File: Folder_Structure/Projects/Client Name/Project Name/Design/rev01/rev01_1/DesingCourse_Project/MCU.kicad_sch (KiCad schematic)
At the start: 43 parts, among them J3 874380243, J4 874380843, J5 874380343, J6 874380643, U3 STM32F405RGTx, Y1 8MHz

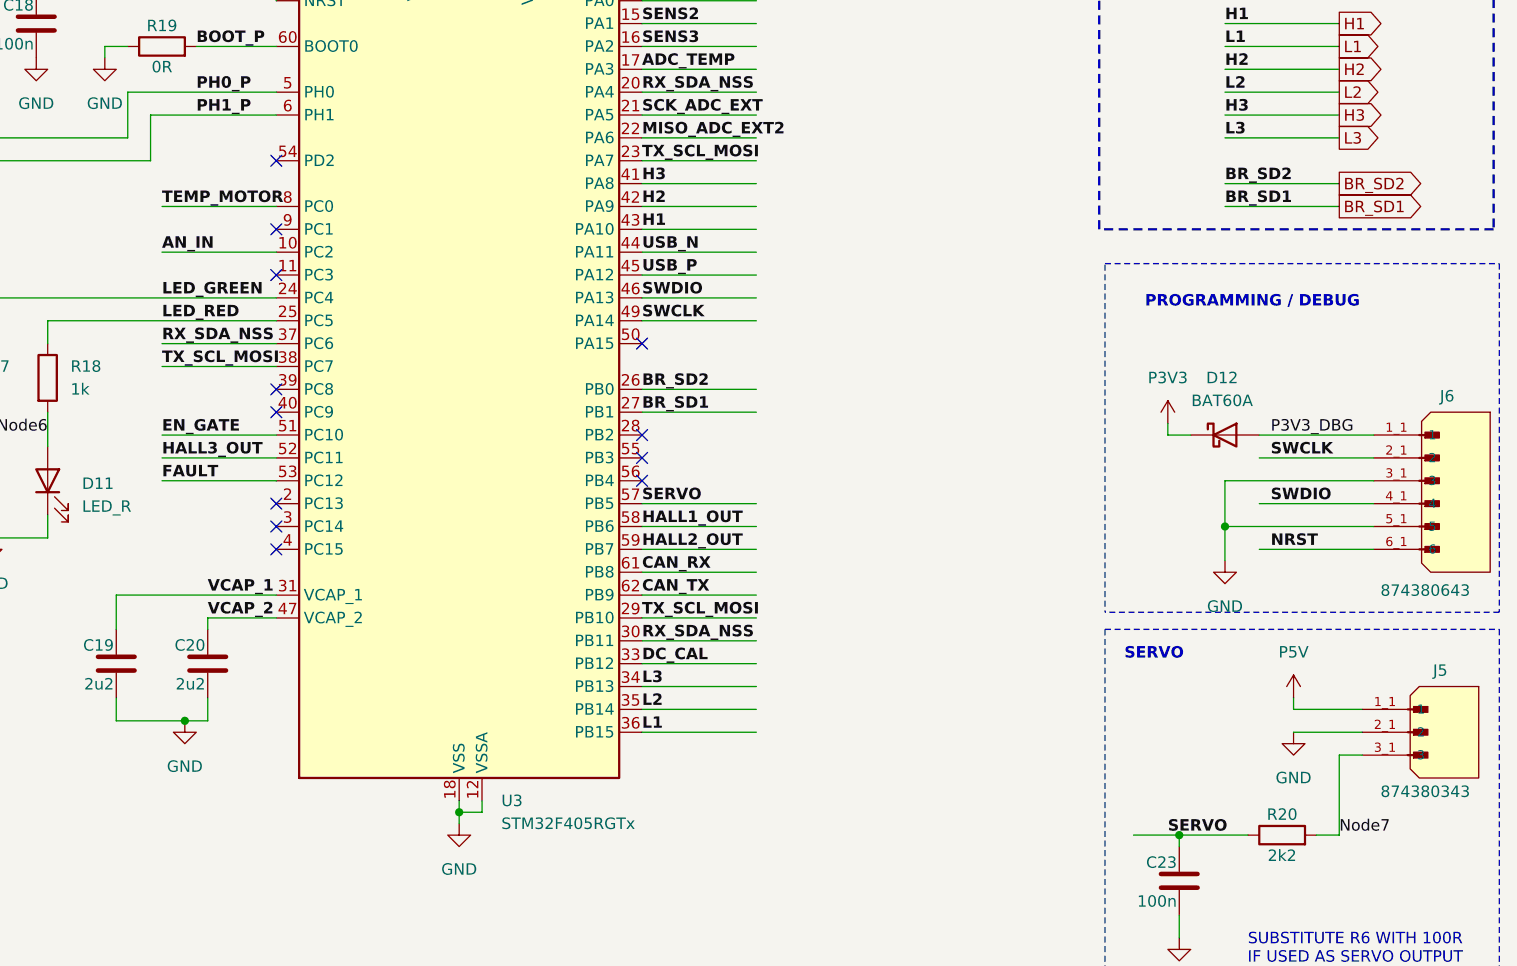
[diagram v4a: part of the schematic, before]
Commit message: Update18
Layout finished, clean up or layout and designators.
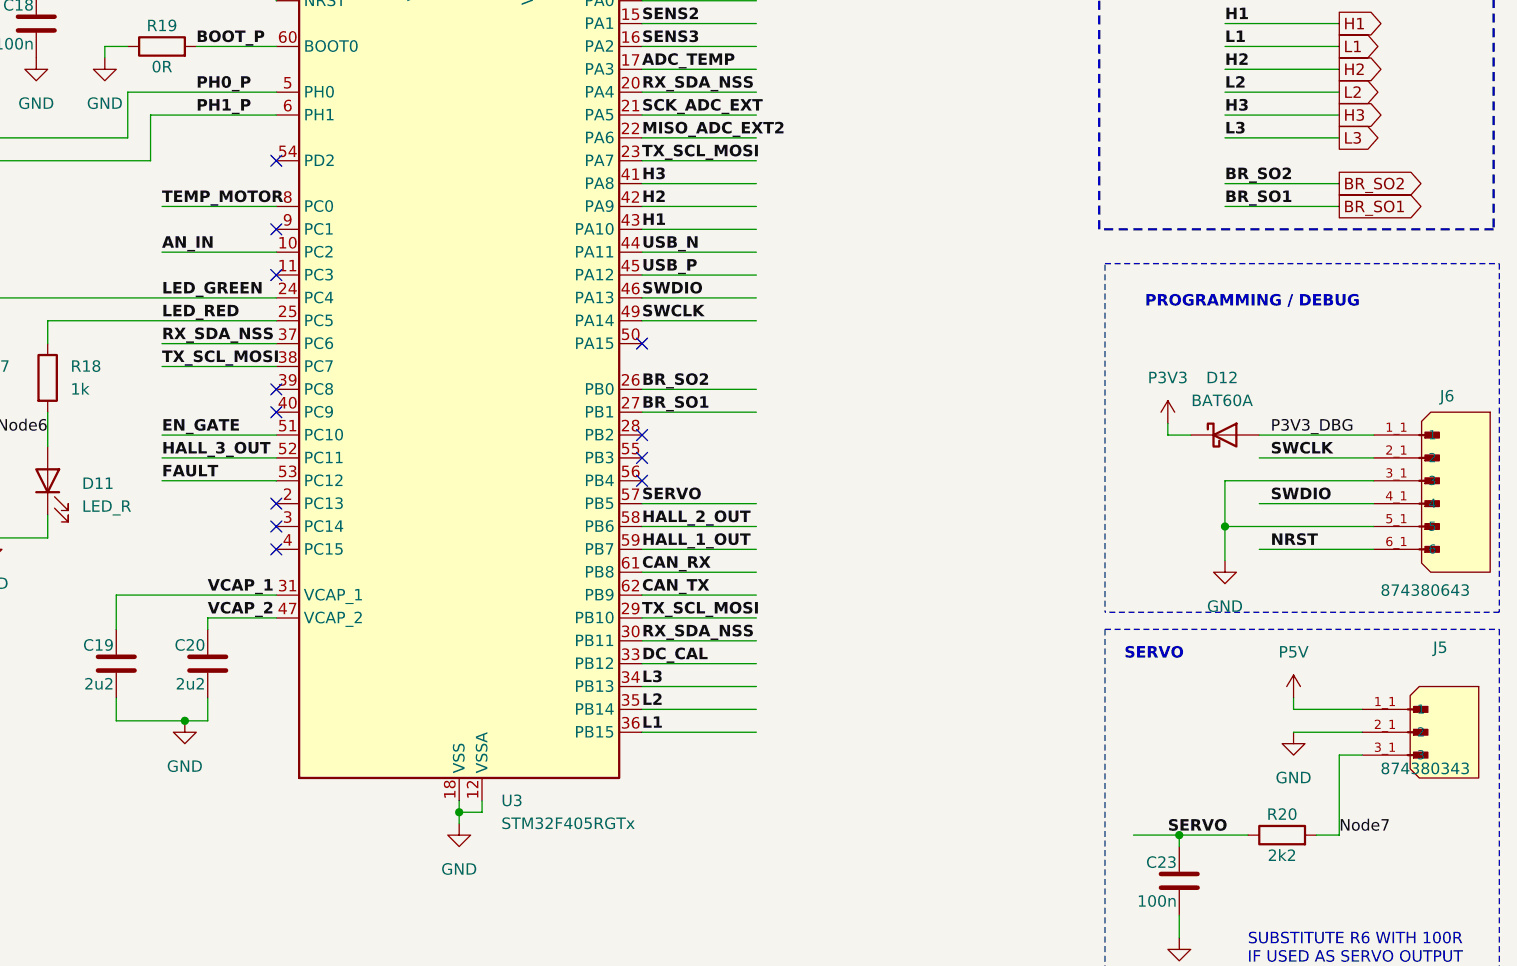
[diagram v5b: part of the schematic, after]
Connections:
- net HALL1_OUT is gone; now on net HALL_2_OUT: U3.58 (PB6)
- net HALL2_OUT is gone; now on net HALL_1_OUT: U3.59 (PB7)
- net HALL3_OUT is gone; now on net HALL_3_OUT: U3.52 (PC11)
- net BR_SD1 renamed BR_SO1
- net BR_SD2 renamed BR_SO2
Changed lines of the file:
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@@
 		)
 	)
-	(label "HALL2_OUT"
-		(at 184.15 115.57 0)
-		(effects
-			(font
-				(size 1.27 1.27)
-				(thickness 0.254)
-				(bold yes)
-			)
-			(justify left bottom)
-		)
-	)
 	(label "L2"
 		(at 184.15 133.35 0)
@@
 		)
 	)
-	(label "BR_SD2"
+	(label "BR_SO2"
 		(at 184.15 97.79 0)
 		(effects
@@
 		)
 	)
-	(label "BR_SD2"
+	(label "BR_SO2"
 		(at 248.92 74.93 0)
 		(effects
@@
 		)
 	)
-	(label "CAN_TX"
-		(at 248.92 35.56 0)
+	(label "HALL_2_OUT"
+		(at 184.15 113.03 0)
 		(effects
 			(font
@@
 		)
 	)
-	(label "PH1_P"
-		(at 134.62 67.31 0)
+	(label "CAN_TX"
+		(at 248.92 35.56 0)
 		(effects
 			(font
@@
 		)
 	)
-	(label "HALL3_OUT"
-		(at 130.81 105.41 0)
+	(label "PH1_P"
+		(at 134.62 67.31 0)
 		(effects
 			(font
@@
 		)
 	)
-	(label "L1"
-		(at 248.92 59.69 0)
+	(label "HALL_3_OUT"
+		(at 130.81 105.41 0)
 		(effects
 			(font
@@
 		)
 	)
-	(label "BR_SD1"
-		(at 248.92 77.47 0)
+	(label "L1"
+		(at 248.92 59.69 0)
 		(effects
 			(font
@@
 		)
 	)
-	(label "HALL1_OUT"
-		(at 184.15 113.03 0)
+	(label "BR_SO1"
+		(at 248.92 77.47 0)
 		(effects
 			(font
@@
 		)
 	)
-	(label "BR_SD1"
+	(label "BR_SO1"
 		(at 184.15 100.33 0)
 		(effects
@@
 		)
 	)
+	(label "HALL_1_OUT"
+		(at 184.15 115.57 0)
+		(effects
+			(font
+				(size 1.27 1.27)
+				(thickness 0.254)
+				(bold yes)
+			)
+			(justify left bottom)
+		)
+	)
 	(label "H3"
 		(at 248.92 67.31 0)
@@
 		)
 	)
-	(global_label "BR_SD2"
+	(global_label "BR_SO2"
 		(shape output)
 		(at 261.62 74.93 0)
@@
 		)
 		(property "Intersheetrefs" "${INTERSHEET_REFS}"
-			(at 271.8969 74.93 0)
+			(at 271.9574 74.93 0)
 			(effects
 				(font
@@
 		)
 	)
-	(global_label "BR_SD1"
+	(global_label "BR_SO1"
 		(shape output)
 		(at 261.62 77.47 0)
@@
 		)
 		(property "Intersheetrefs" "${INTERSHEET_REFS}"
-			(at 271.8969 77.47 0)
+			(at 271.9574 77.47 0)
 			(effects
 				(font
@@
 			)
 		)
-		(property "Description" "RES 0 OHM 0603 ±1% 1/10W"
+		(property "Description" "Resistor"
 			(at 99.06 90.17 0)
 			(effects
@@
 			)
 		)
-		(property "Description" "LED RED CLEAR 1206 SMD"
+		(property "Description" "Light emitting diode"
 			(at 118.11 107.95 0)
 			(effects
@@
 			)
 		)
-		(property "Description" "CAP CER 0.1UF 10V X7R 0603"
+		(property "Description" "Unpolarized capacitor"
 			(at 67.31 48.26 0)
 			(effects
@@
 			)
 		)
-		(property "Description" "CAP CER 0.1UF 10V X7R 0603"
+		(property "Description" "Unpolarized capacitor"
 			(at 93.98 48.26 0)
 			(effects
@@
 			)
 		)
-		(property "Description" "RES 0 OHM 0603 ±1% 1/10W"
+		(property "Description" "Resistor"
 			(at 130.81 59.69 0)
 			(effects
@@
 			)
 		)
-		(property "Description" "CAP CER 0.1UF 10V X7R 0603"
+		(property "Description" "Unpolarized capacitor"
 			(at 83.82 48.26 0)
 			(effects
@@
 			)
 		)
-		(property "Description" "SWITCH TACTILE SPST-NO 0.05A 12V"
+		(property "Description" "1x DIP Switch, Single Pole Single Throw (SPST) switch, small symbol"
 			(at 106.68 50.8 0)
 			(effects
@@
 			)
 		)
-		(property "Description" "RES 39k OHM 0603 ±1% 1/10W"
+		(property "Description" "Resistor"
 			(at 22.86 142.24 0)
 			(effects
@@
 			)
 		)
-		(property "Description" "THERMISTOR NTC 10KOHM 3380K 0603"
+		(property "Description" "Temperature dependent resistor, negative temperature coefficient"
 			(at 35.56 106.68 0)
 			(effects
@@
 			)
 		)
-		(property "Description" "CAP CER 10PF 50V C0G/NP0 0603"
+		(property "Description" "Unpolarized capacitor"
 			(at 86.36 69.85 0)
 			(effects
@@
 			)
 		)
-		(property "Description" "CAP CER 0.1UF 10V X7R 0603"
+		(property "Description" "Unpolarized capacitor"
 			(at 88.9 48.26 0)
 			(effects
@@
 			)
 		)
-		(property "Description" "CAP CER 2.2UF 6.3V X5R 0603"
+		(property "Description" "Unpolarized capacitor"
 			(at 125.73 128.27 0)
 			(effects
@@
 			)
 		)
-		(property "Description" "CAP CER 0.1UF 10V X7R 0603"
+		(property "Description" "Unpolarized capacitor"
 			(at 194.31 38.1 0)
 			(effects
@@
 			)
 		)
-		(property "Description" "RES 0 OHM 0603 ±1% 1/10W"
+		(property "Description" "Resistor"
 			(at 99.06 69.85 0)
 			(effects
@@
 			)
 		)
-		(property "Description" "RES 1k OHM 0603 ±1% 1/10W"
+		(property "Description" "Resistor"
 			(at 107.95 96.52 0)
 			(effects
@@
 			)
 		)
-		(property "Description" "CAP CER 1UF 10V X5R 0603"
+		(property "Description" "Unpolarized capacitor"
 			(at 207.01 38.1 0)
 			(effects
@@
 			)
 		)
-		(property "Description" "CAP CER 2.2UF 6.3V X5R 0603"
+		(property "Description" "Unpolarized capacitor"
 			(at 135.89 128.27 0)
 			(effects
@@
 			)
 		)
-		(property "Description" "CAP CER 0.1UF 10V X7R 0603"
+		(property "Description" "Unpolarized capacitor"
 			(at 73.66 48.26 0)
 			(effects
@@
 			)
 		)
-		(property "Description" "RES 2k2 OHM 0603 ±1% 1/10W"
+		(property "Description" "Resistor"
 			(at 35.56 88.9 0)
 			(effects
@@
 			)
 		)
-		(property "Description" "RES 2k2 OHM 0603 ±1% 1/10W"
+		(property "Description" "Resistor"
 			(at 22.86 152.4 0)
 			(effects
@@
 			)
 		)
-		(property "Description" "CAP CER 10PF 50V C0G/NP0 0603"
+		(property "Description" "Unpolarized capacitor"
 			(at 86.36 90.17 0)
 			(effects
@@
 			)
 		)
-		(property "Description" "RES 2k2 OHM 0603 ±1% 1/10W"
+		(property "Description" "Resistor"
 			(at 255.27 147.32 0)
 			(effects
@@
 			)
 		)
-		(property "Description" "RES 1k OHM 0603 ±1% 1/10W"
+		(property "Description" "Resistor"
 			(at 118.11 96.52 0)
 			(effects
@@
 			)
 		)
-		(property "Description" "CAP CER 0.1UF 10V X7R 0603"
+		(property "Description" "Unpolarized capacitor"
 			(at 116.84 57.15 0)
 			(effects
@@
 	)
 	(symbol
-		(lib_name "PESD3V3U1UA_115_1")
 		(lib_id "PESD3V3U1UA_115:PESD3V3U1UA_115")
 		(at 66.04 185.42 90)
@@
 			)
 		)
-		(property "Description" "CAP CER 0.1UF 10V X7R 0603"
+		(property "Description" "Unpolarized capacitor"
 			(at 36.83 152.4 0)
 			(effects
@@
 			)
 		)
-		(property "Description" "CAP CER 0.1UF 10V X7R 0603"
+		(property "Description" "Unpolarized capacitor"
 			(at 243.84 152.4 0)
 			(effects
@@
 	(symbol
 		(lib_id "Molex_87438:874380343")
-		(at 269.24 135.89 0)
+		(at 269.24 133.35 0)
 		(unit 1)
 		(exclude_from_sim no)
@@
 		(dnp no)
 		(property "Reference" "J5"
-			(at 272.034 129.032 0)
+			(at 272.034 126.492 0)
 			(effects
 				(font
@@
 		)
 		(property "Value" "874380343"
-			(at 266.192 142.494 0)
+			(at 266.192 139.954 0)
 			(effects
 				(font
@@
 		)
 		(property "Footprint" "874380843:MOLEX_874380343"
-			(at 269.494 136.652 0)
+			(at 269.494 134.112 0)
 			(effects
 				(font
@@
 		)
 		(property "Datasheet" ""
-			(at 269.24 135.89 0)
+			(at 269.24 133.35 0)
 			(effects
 				(font
@@
 		)
 		(property "Description" "Conn Shrouded Header HDR 3 POS 1.5mm Solder RA Side Entry SMD Pico-SPOX™ T/R"
-			(at 269.494 136.652 0)
+			(at 269.494 134.112 0)
 			(effects
 				(font
@@
 		)
 		(property "Manufacturer" "Molex"
-			(at 269.494 136.652 0)
+			(at 269.494 134.112 0)
 			(effects
 				(font
@@
 		)
 		(property "MAXIMUM_PACKAGE_HEIGHT" "4.45 mm"
-			(at 269.494 136.398 0)
+			(at 269.494 133.858 0)
 			(effects
 				(font
@@
 		)
 		(property "Package" "SMT"
-			(at 269.24 136.652 0)
+			(at 269.24 134.112 0)
 			(effects
 				(font
@@
 		)
 		(property "MPN" "874380343"
-			(at 269.494 136.398 0)
+			(at 269.494 133.858 0)
 			(effects
 				(font
@@
 		)
 		(property "MNP" ""
-			(at 269.24 135.89 0)
+			(at 269.24 133.35 0)
 			(effects
 				(font
@@
 		)
 		(property "MF" ""
-			(at 269.24 135.89 0)
+			(at 269.24 133.35 0)
 			(effects
 				(font
@@
 		)
 		(instances
-			(project ""
+			(project "DesingCourse_Project"
 				(path "/e63e39d7-6ac0-4ffd-8aa3-1841a4541b55/c582aa5b-bceb-43c7-823e-4bc027bffba3"
 					(reference "J5")
@@
 			)
 		)
-		(property "Description" "LED GREEN CLEAR 1206 SMD"
+		(property "Description" "Light emitting diode"
 			(at 107.95 107.95 0)
 			(effects
@@
 			)
 		)
-		(property "Description" "CAP CER 0.1UF 10V X7R 0603"
+		(property "Description" "Unpolarized capacitor"
 			(at 78.74 48.26 0)
 			(effects
@@
 			)
 		)
-		(property "Description" "CAP CER 0.1UF 10V X7R 0603"
+		(property "Description" "Unpolarized capacitor"
 			(at 48.26 88.9 0)
 			(effects
@@
 			)
 		)
-		(property "Description" "RES 2k2 OHM 0603 ±1% 1/10W"
+		(property "Description" "Resistor"
 			(at 99.06 55.88 0)
 			(effects
@@
 			)
 		)
-		(property "Description" "FERRITE BEAD 120 OHM 0603 1LN"
+		(property "Description" "Ferrite bead"
 			(at 220.98 31.75 0)
 			(effects
@@
 			)
 		)
-		(property "Description" "CAP CER 10UF 10V X5R 0603"
+		(property "Description" "Unpolarized capacitor"
 			(at 54.61 48.26 0)
 			(effects
